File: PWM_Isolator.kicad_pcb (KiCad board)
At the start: 2 copper layers, 27.9 x 36.1 mm, 12 parts, among them P1 GND_IN_1, P10 NC, P2 GND_IN_2, P3 Pololu PWM + Power rail, P4 PWM_OUT_1, P5 PWM_OUT_2, P6 Motor_Pwr1, P7 Motor_Pwr2, P8 Motor PWR, P9 Motor PWR, U1 Si8660BA-B-IS1, U2 Si8660BA-B-IS1

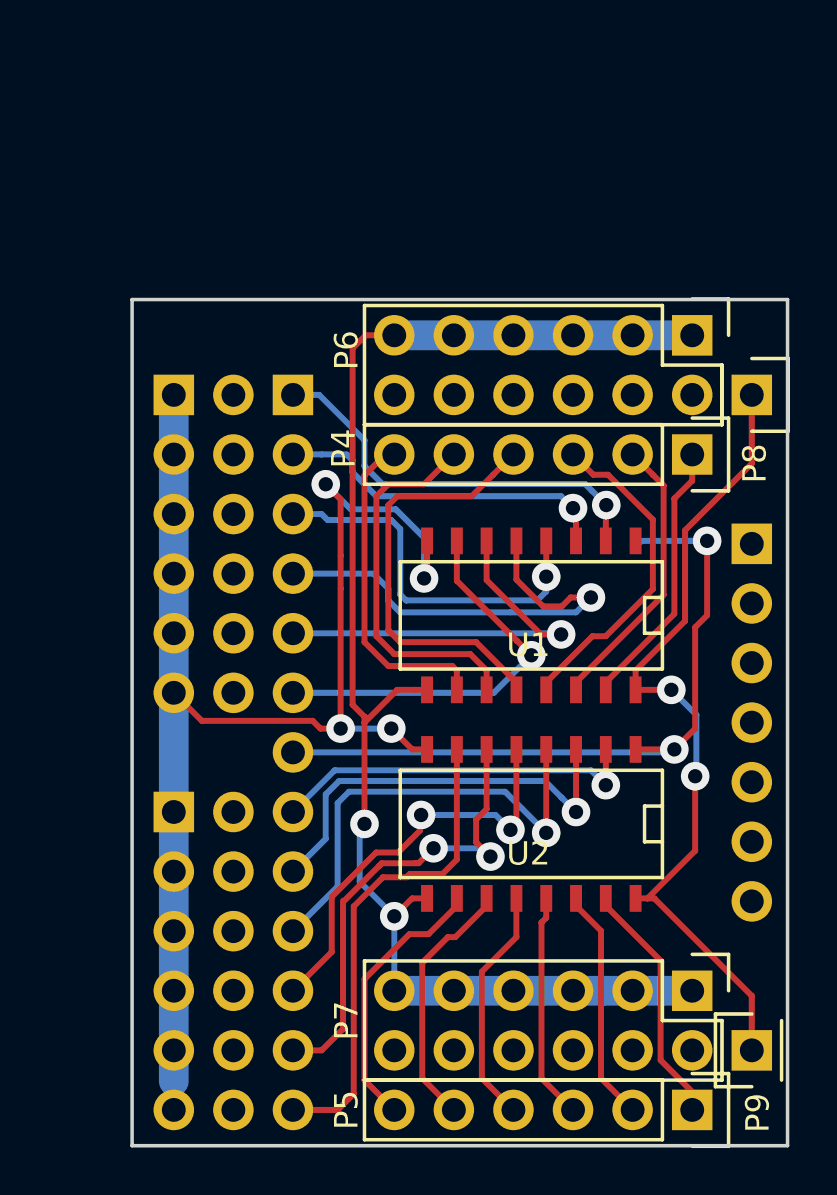
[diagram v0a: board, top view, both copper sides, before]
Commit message: Change footprint of Si8660 and re-route the PCB.
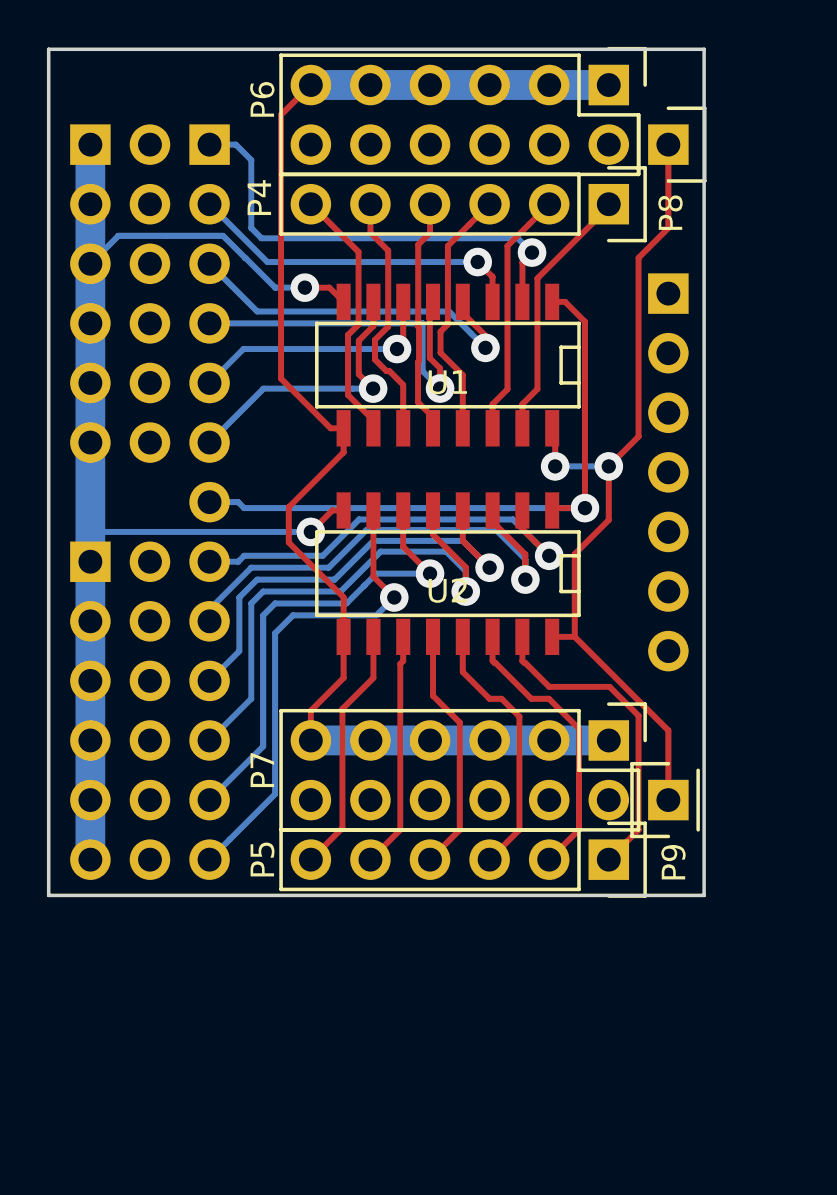
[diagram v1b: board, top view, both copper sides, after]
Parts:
- U1, U2: footprint SMD_Packages:SO-16-N -> Zeabus:Narrow-SOIC-16
- moved P10 11.2 mm to (159.0, 92.2)
- moved P4 11.2 mm to (156.5, 88.4)
- moved P5 11.2 mm to (156.5, 116.3)
- moved P6 11.2 mm to (156.5, 83.3)
- moved P7 11.2 mm to (156.5, 111.3)
- moved U1 11.2 mm to (149.6, 95.2)
- moved U2 11.2 mm to (149.6, 104.1)
- moved P3 11.2 mm to (139.4, 85.9)
- moved P8 11.2 mm to (159.0, 85.9)
- moved P9 11.2 mm to (159.0, 113.8)
- moved P1 11.2 mm to (134.4, 85.9)
- moved P2 11.2 mm to (134.4, 103.6)
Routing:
- net Net-(P4-Pad4): track 18.3 -> 10.1 mm
- net Net-(P3-Pad5): track 17.3 -> 10.7 mm
- net GNDA: track 61.5 -> 55.5 mm, vias 4 -> 2
- net Net-(P4-Pad5): track 16.1 -> 10.7 mm
- net Net-(P3-Pad6): track 17.0 -> 12.1 mm
- net Net-(P3-Pad11): track 17.9 -> 21.9 mm, vias 2 -> 1
- net Net-(P3-Pad4): track 19.4 -> 16.1 mm
- net +5VA: track 30.5 -> 27.2 mm, vias 2 -> 1
- net Net-(P4-Pad3): track 14.0 -> 10.8 mm
- net Net-(P5-Pad1): track 10.5 -> 13.6 mm
- net Net-(P4-Pad6): track 14.0 -> 11.0 mm
- net GNDD: track 60.7 -> 57.8 mm, vias 2 -> 0
- net Net-(P3-Pad8): track 15.9 -> 18.3 mm
- net Net-(P3-Pad9): track 18.0 -> 20.3 mm
- net Net-(P3-Pad1): track 17.5 -> 19.6 mm
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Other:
- board text added: "1.0.0"
- board text added: "8 March 2017"
- board text added: "PWM Isolator"
